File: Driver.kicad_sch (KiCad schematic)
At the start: 18 parts, among them U1 IRS21867S, U2 IRS21867S, U8 IRS21867S

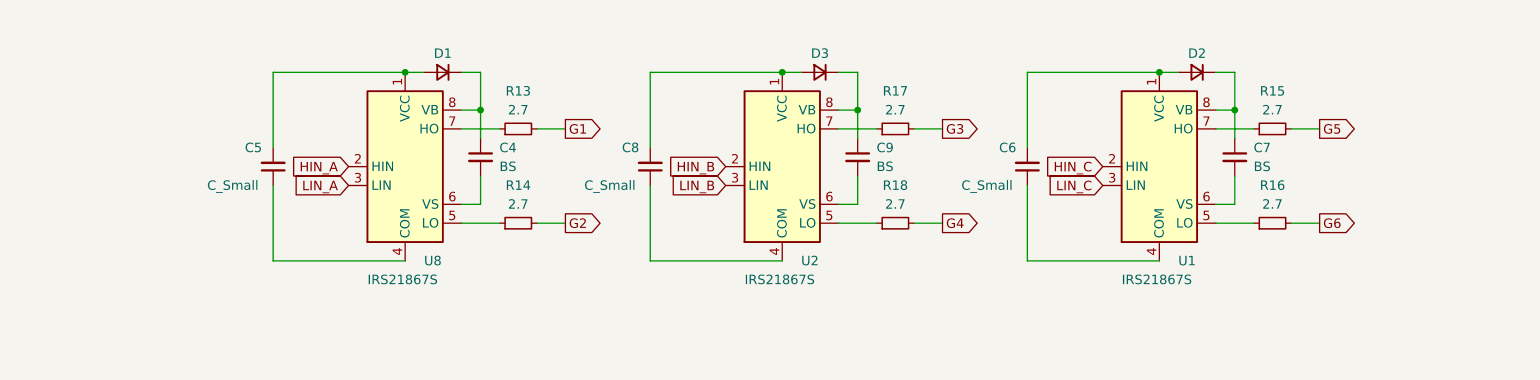
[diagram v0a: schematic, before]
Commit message: Добавил шунты
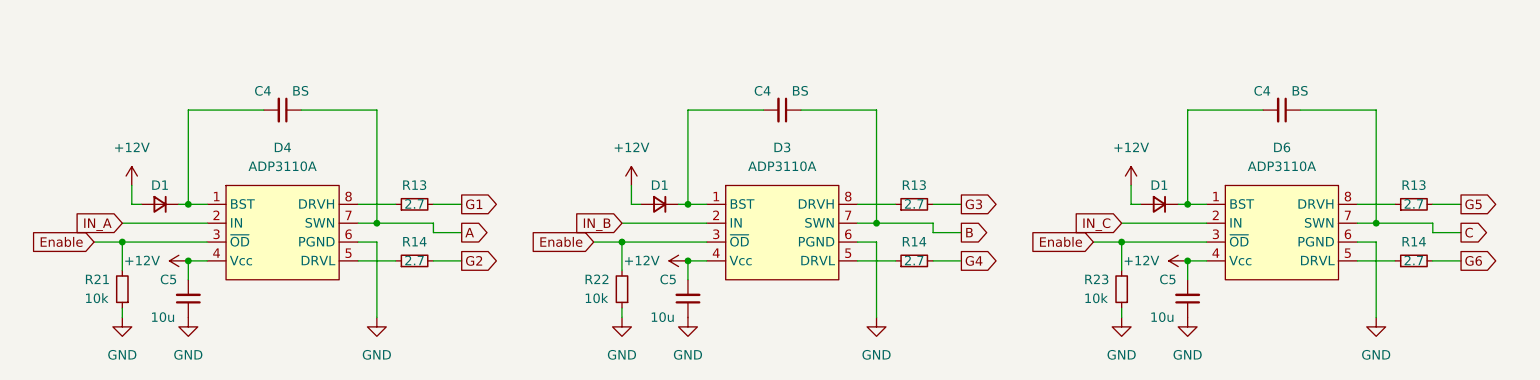
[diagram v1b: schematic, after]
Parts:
- removed C6, C8: C_Small, Capacitor_SMD:C_0805_2012Metric_Pad1.18x1.45mm_HandSolder, symbol Device:C_Small
- removed C7, C9: BS, Capacitor_SMD:C_0805_2012Metric_Pad1.18x1.45mm_HandSolder, symbol Device:C_Small
- removed D2, D3: D_Small, Diode_SMD:D_SOD-323, symbol Device:D_Small
- removed R15, R16, R17, R18: 2.7, Resistor_SMD:R_1206_3216Metric_Pad1.30x1.75mm_HandSolder, symbol Device:R_Small
- removed U1, U2, U8: IRS21867S, Package_SO:SOIC-8_3.9x4.9mm_P1.27mm, symbol Driver_FET:IRS21867S
- added C4 (x2): BS, Capacitor_SMD:C_0805_2012Metric_Pad1.18x1.45mm_HandSolder, symbol Device:C_Small
- added C5 (x2): 10u, Capacitor_SMD:C_0805_2012Metric_Pad1.18x1.45mm_HandSolder, symbol Device:C_Small
- added D1 (x2): D_Small, Diode_SMD:D_SOD-323, symbol Device:D_Small
- added D3, D4, D6: ADP3110A, Package_DFN_QFN:DFN-8-1EP_3x3mm_P0.65mm_EP1.7x2.05mm, symbol IGBT_MOSFET_Drivers:ADP3110A
- added R13 (x2), R14 (x2): 2.7, Resistor_SMD:R_1206_3216Metric_Pad1.30x1.75mm_HandSolder, symbol Device:R_Small
- added R21, R22, R23: 10k, Resistor_SMD:R_0805_2012Metric_Pad1.20x1.40mm_HandSolder, symbol Device:R_Small
- C5: value C_Small -> 10u
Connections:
- net G3: now also R13.2
- net G4: now also R14.2
- net G5: now also R13.2
- net G6: now also R14.2
- net at D1.1 (K): now also C4.2, D4.1 (BST); no longer C4.1
- net +12V: now reaches C5.2, D1.2 (A)
- net +12V: now also C5.2, C5.2, D1.2 (A), D1.2 (A), D3.4 (Vcc), D4.4 (Vcc), D6.4 (Vcc)
- net at R13.1: now also D4.8 (DRVH)
- net at R14.1: now also D4.5 (DRVL)
- net GND: now reaches C5.1
- net GND: now also C5.1, C5.1, D3.6 (PGND), D4.6 (PGND), D6.6 (PGND), R21.1, R22.1, R23.1
- new net: D6.5 (DRVL), R14.1
- new net: C4.2, D1.1 (K), D6.1 (BST)
- new net: D6.8 (DRVH), R13.1
- new net: C4.2, D1.1 (K), D3.1 (BST)
- new net: D3.8 (DRVH), R13.1
- new net: D3.5 (DRVL), R14.1
- new net A: C4.1, D4.7 (SWN)
- new net B: C4.1, D3.7 (SWN)
- new net C: C4.1, D6.7 (SWN)
- new net Enable: D3.3 (~{OD}), D4.3 (~{OD}), D6.3 (~{OD}), R21.2, R22.2, R23.2
- new net IN_A: D4.2 (IN)
- new net IN_B: D3.2 (IN)
- new net IN_C: D6.2 (IN)
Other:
- moved on the sheet: C4, C5, D1, R13, R14

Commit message: Стартовый вариант
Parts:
- R13, R14: footprint Resistor_SMD:R_1206_3216Metric_Pad1.30x1.75mm_HandSolder -> Resistor_SMD:R_0805_2012Metric_Pad1.20x1.40mm_HandSolder
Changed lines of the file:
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@@
       (effects (font (size 1.27 1.27)))
     )
-    (property "Footprint" "Resistor_SMD:R_1206_3216Metric_Pad1.30x1.75mm_HandSolder" (at 231.14 102.87 0)
+    (property "Footprint" "Resistor_SMD:R_0805_2012Metric_Pad1.20x1.40mm_HandSolder" (at 231.14 102.87 0)
       (effects (font (size 1.27 1.27)) hide)
     )
@@
       (effects (font (size 1.27 1.27)))
     )
-    (property "Footprint" "Resistor_SMD:R_1206_3216Metric_Pad1.30x1.75mm_HandSolder" (at 231.14 95.25 0)
+    (property "Footprint" "Resistor_SMD:R_0805_2012Metric_Pad1.20x1.40mm_HandSolder" (at 231.14 95.25 0)
       (effects (font (size 1.27 1.27)) hide)
     )
@@
       (effects (font (size 1.27 1.27)))
     )
-    (property "Footprint" "Resistor_SMD:R_1206_3216Metric_Pad1.30x1.75mm_HandSolder" (at 96.52 95.25 0)
+    (property "Footprint" "Resistor_SMD:R_0805_2012Metric_Pad1.20x1.40mm_HandSolder" (at 96.52 95.25 0)
       (effects (font (size 1.27 1.27)) hide)
     )
@@
       (effects (font (size 1.27 1.27)))
     )
-    (property "Footprint" "Resistor_SMD:R_1206_3216Metric_Pad1.30x1.75mm_HandSolder" (at 163.83 95.25 0)
+    (property "Footprint" "Resistor_SMD:R_0805_2012Metric_Pad1.20x1.40mm_HandSolder" (at 163.83 95.25 0)
       (effects (font (size 1.27 1.27)) hide)
     )
@@
       (effects (font (size 1.27 1.27)))
     )
-    (property "Footprint" "Resistor_SMD:R_1206_3216Metric_Pad1.30x1.75mm_HandSolder" (at 96.52 102.87 0)
+    (property "Footprint" "Resistor_SMD:R_0805_2012Metric_Pad1.20x1.40mm_HandSolder" (at 96.52 102.87 0)
       (effects (font (size 1.27 1.27)) hide)
     )
@@
       (effects (font (size 1.27 1.27)))
     )
-    (property "Footprint" "Resistor_SMD:R_1206_3216Metric_Pad1.30x1.75mm_HandSolder" (at 163.83 102.87 0)
-      (effects (font (size 1.27 1.27)) hide)
-    )
+    (property "Footprint" "Resistor_SMD:R_0805_2012Metric_Pad1.20x1.40mm_HandSolder" (at 163.83 102.87 0)
+      (effects (font (size 1.27 1.27)) hide)
+    )

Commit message: Стартовая версия
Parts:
- removed R22, R23: 10k, Resistor_SMD:R_0805_2012Metric_Pad1.20x1.40mm_HandSolder, symbol Device:R_Small
- added R10, R11, R6, R7, R8, R9: 10k, Resistor_SMD:R_0805_2012Metric_Pad1.20x1.40mm_HandSolder, symbol Device:R_Small
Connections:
- net A: now also R6.1
- net B: now also R8.1
- net C: now also R10.1
- net G1: now also R6.2
- net G2: now also R7.2
- net G3: now also R8.2
- net G4: now also R9.2
- net G5: now also R10.2
- net G6: now also R11.2
- net GND: now also R11.1, R7.1, R9.1

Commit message: Стартовая версия
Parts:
- removed C4 (x3): BS, Capacitor_SMD:C_0805_2012Metric_Pad1.18x1.45mm_HandSolder, symbol Device:C_Small
- removed C5 (x3): 10u, Capacitor_SMD:C_0805_2012Metric_Pad1.18x1.45mm_HandSolder, symbol Device:C_Small
- removed D1 (x3): D_Small, Diode_SMD:D_SOD-323, symbol Device:D_Small
- removed D3, D4, D6: ADP3110A, Package_DFN_QFN:DFN-8-1EP_3x3mm_P0.65mm_EP1.7x2.05mm, symbol IGBT_MOSFET_Drivers:ADP3110A
- removed R13 (x3), R14 (x3): 2.7, Resistor_SMD:R_0805_2012Metric_Pad1.20x1.40mm_HandSolder, symbol Device:R_Small
- removed R21: 10k, Resistor_SMD:R_0805_2012Metric_Pad1.20x1.40mm_HandSolder, symbol Device:R_Small
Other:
- moved on the sheet: R10, R11, R6, R7, R8, R9

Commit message: Стартовая версия
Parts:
- renumbered R6 to R3, R7 to R4, R8 to R5, R9 to R6, R10 to R7, R11 to R8
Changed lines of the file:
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@@
   (symbol (lib_id "Device:R_Small") (at 144.78 106.68 180) (unit 1)
     (in_bom yes) (on_board yes) (dnp no)
-    (property "Reference" "R9" (at 139.7 105.41 0)
+    (property "Reference" "R6" (at 139.7 105.41 0)
       (effects (font (size 1.27 1.27)) (justify right))
     )
@@
       (project "Силовая плата"
         (path "/96c6fc92-8ec6-44f7-b0dc-9ad8f1acea09/6f5415fb-38ca-4d8b-9553-51f9710fbbb5"
-          (reference "R9") (unit 1)
+          (reference "R6") (unit 1)
         )
       )
@@
   (symbol (lib_id "Device:R_Small") (at 144.78 95.25 180) (unit 1)
     (in_bom yes) (on_board yes) (dnp no)
-    (property "Reference" "R8" (at 139.7 93.98 0)
+    (property "Reference" "R5" (at 139.7 93.98 0)
       (effects (font (size 1.27 1.27)) (justify right))
     )
@@
       (project "Силовая плата"
         (path "/96c6fc92-8ec6-44f7-b0dc-9ad8f1acea09/6f5415fb-38ca-4d8b-9553-51f9710fbbb5"
+          (reference "R5") (unit 1)
+        )
+      )
+    )
+  )
+  (symbol (lib_id "Device:R_Small") (at 212.09 106.68 180) (unit 1)
+    (in_bom yes) (on_board yes) (dnp no)
+    (property "Reference" "R8" (at 207.01 105.41 0)
+      (effects (font (size 1.27 1.27)) (justify right))
+    )
+    (property "Value" "10k" (at 207.01 107.95 0)
+      (effects (font (size 1.27 1.27)) (justify right))
+    )
+    (property "Footprint" "Resistor_SMD:R_0805_2012Metric_Pad1.20x1.40mm_HandSolder" (at 212.09 106.68 0)
+      (effects (font (size 1.27 1.27)) hide)
+    )
+    (property "Datasheet" "~" (at 212.09 106.68 0)
+      (effects (font (size 1.27 1.27)) hide)
+    )
+    (pin "1")
+    (pin "2")
+    (instances
+      (project "Силовая плата"
+        (path "/96c6fc92-8ec6-44f7-b0dc-9ad8f1acea09/6f5415fb-38ca-4d8b-9553-51f9710fbbb5"
           (reference "R8") (unit 1)
-        )
-      )
-    )
-  )
-  (symbol (lib_id "Device:R_Small") (at 212.09 106.68 180) (unit 1)
-    (in_bom yes) (on_board yes) (dnp no)
-    (property "Reference" "R11" (at 207.01 105.41 0)
-      (effects (font (size 1.27 1.27)) (justify right))
-    )
-    (property "Value" "10k" (at 207.01 107.95 0)
-      (effects (font (size 1.27 1.27)) (justify right))
-    )
-    (property "Footprint" "Resistor_SMD:R_0805_2012Metric_Pad1.20x1.40mm_HandSolder" (at 212.09 106.68 0)
-      (effects (font (size 1.27 1.27)) hide)
-    )
-    (property "Datasheet" "~" (at 212.09 106.68 0)
-      (effects (font (size 1.27 1.27)) hide)
-    )
-    (pin "1")
-    (pin "2")
-    (instances
-      (project "Силовая плата"
-        (path "/96c6fc92-8ec6-44f7-b0dc-9ad8f1acea09/6f5415fb-38ca-4d8b-9553-51f9710fbbb5"
-          (reference "R11") (unit 1)
         )
       )
@@
   (symbol (lib_id "power:GND") (at 78.74 110.49 90) (unit 1)
     (in_bom yes) (on_board yes) (dnp no) (fields_autoplaced)
-    (property "Reference" "#PWR047" (at 85.09 110.49 0)
+    (property "Reference" "#PWR03" (at 85.09 110.49 0)
       (effects (font (size 1.27 1.27)) hide)
     )
@@
       (project "Силовая плата"
         (path "/96c6fc92-8ec6-44f7-b0dc-9ad8f1acea09/6f5415fb-38ca-4d8b-9553-51f9710fbbb5"
-          (reference "#PWR047") (unit 1)
+          (reference "#PWR03") (unit 1)
         )
       )
@@
   (symbol (lib_id "power:GND") (at 146.05 110.49 90) (unit 1)
     (in_bom yes) (on_board yes) (dnp no) (fields_autoplaced)
-    (property "Reference" "#PWR048" (at 152.4 110.49 0)
+    (property "Reference" "#PWR04" (at 152.4 110.49 0)
       (effects (font (size 1.27 1.27)) hide)
     )
@@
       (project "Силовая плата"
         (path "/96c6fc92-8ec6-44f7-b0dc-9ad8f1acea09/6f5415fb-38ca-4d8b-9553-51f9710fbbb5"
-          (reference "#PWR048") (unit 1)
+          (reference "#PWR04") (unit 1)
         )
       )
@@
   (symbol (lib_id "Device:R_Small") (at 77.47 106.68 180) (unit 1)
     (in_bom yes) (on_board yes) (dnp no)
-    (property "Reference" "R7" (at 72.39 105.41 0)
+    (property "Reference" "R4" (at 72.39 105.41 0)
       (effects (font (size 1.27 1.27)) (justify right))
     )
@@
       (project "Силовая плата"
         (path "/96c6fc92-8ec6-44f7-b0dc-9ad8f1acea09/6f5415fb-38ca-4d8b-9553-51f9710fbbb5"
+          (reference "R4") (unit 1)
+        )
+      )
+    )
+  )
+  (symbol (lib_id "Device:R_Small") (at 212.09 95.25 180) (unit 1)
+    (in_bom yes) (on_board yes) (dnp no)
+    (property "Reference" "R7" (at 207.01 93.98 0)
+      (effects (font (size 1.27 1.27)) (justify right))
+    )
+    (property "Value" "10k" (at 207.01 96.52 0)
+      (effects (font (size 1.27 1.27)) (justify right))
+    )
+    (property "Footprint" "Resistor_SMD:R_0805_2012Metric_Pad1.20x1.40mm_HandSolder" (at 212.09 95.25 0)
+      (effects (font (size 1.27 1.27)) hide)
+    )
+    (property "Datasheet" "~" (at 212.09 95.25 0)
+      (effects (font (size 1.27 1.27)) hide)
+    )
+    (pin "1")
+    (pin "2")
+    (instances
+      (project "Силовая плата"
+        (path "/96c6fc92-8ec6-44f7-b0dc-9ad8f1acea09/6f5415fb-38ca-4d8b-9553-51f9710fbbb5"
           (reference "R7") (unit 1)
-        )
-      )
-    )
-  )
-  (symbol (lib_id "Device:R_Small") (at 212.09 95.25 180) (unit 1)
-    (in_bom yes) (on_board yes) (dnp no)
-    (property "Reference" "R10" (at 207.01 93.98 0)
-      (effects (font (size 1.27 1.27)) (justify right))
-    )
-    (property "Value" "10k" (at 207.01 96.52 0)
-      (effects (font (size 1.27 1.27)) (justify right))
-    )
-    (property "Footprint" "Resistor_SMD:R_0805_2012Metric_Pad1.20x1.40mm_HandSolder" (at 212.09 95.25 0)
-      (effects (font (size 1.27 1.27)) hide)
-    )
-    (property "Datasheet" "~" (at 212.09 95.25 0)
-      (effects (font (size 1.27 1.27)) hide)
-    )
-    (pin "1")
-    (pin "2")
-    (instances
-      (project "Силовая плата"
-        (path "/96c6fc92-8ec6-44f7-b0dc-9ad8f1acea09/6f5415fb-38ca-4d8b-9553-51f9710fbbb5"
-          (reference "R10") (unit 1)
         )
       )
@@
   (symbol (lib_id "power:GND") (at 213.36 110.49 90) (unit 1)
     (in_bom yes) (on_board yes) (dnp no) (fields_autoplaced)
-    (property "Reference" "#PWR049" (at 219.71 110.49 0)
+    (property "Reference" "#PWR05" (at 219.71 110.49 0)
       (effects (font (size 1.27 1.27)) hide)
     )
@@
       (project "Силовая плата"
         (path "/96c6fc92-8ec6-44f7-b0dc-9ad8f1acea09/6f5415fb-38ca-4d8b-9553-51f9710fbbb5"
-          (reference "#PWR049") (unit 1)
+          (reference "#PWR05") (unit 1)
         )
       )
@@
   (symbol (lib_id "Device:R_Small") (at 77.47 95.25 180) (unit 1)
     (in_bom yes) (on_board yes) (dnp no)
-    (property "Reference" "R6" (at 72.39 93.98 0)
+    (property "Reference" "R3" (at 72.39 93.98 0)
       (effects (font (size 1.27 1.27)) (justify right))
     )
@@
       (project "Силовая плата"
         (path "/96c6fc92-8ec6-44f7-b0dc-9ad8f1acea09/6f5415fb-38ca-4d8b-9553-51f9710fbbb5"
-          (reference "R6") (unit 1)
-        )
-      )
+          (reference "R3") (unit 1)
+        )
+      )
